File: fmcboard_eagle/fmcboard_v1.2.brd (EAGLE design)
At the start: 125 x 74 mm, 113 parts, among them IC1 OPA699ID, IC10 LTC6229IMS8E#TRPBF, IC2 LM2662M_NOPB, IC3 LTC6229IMS8E#TRPBF, IC4 LTC6229IMS8E#TRPBF, IC5 LM358, IC6 OPA699ID, IC7 OPA699ID, IC8 LTC6229IMS8E#TRPBF, IC9 LTC6229IMS8E#TRPBF, J1 8pin, J12 4p-2.54, J2 ASP-134604-01, J3 4p-2.54, J4 4p-2.54, J5 8pin, J6 4p-2.54, J7 4p-2.54, U1 TXS0108EPWR

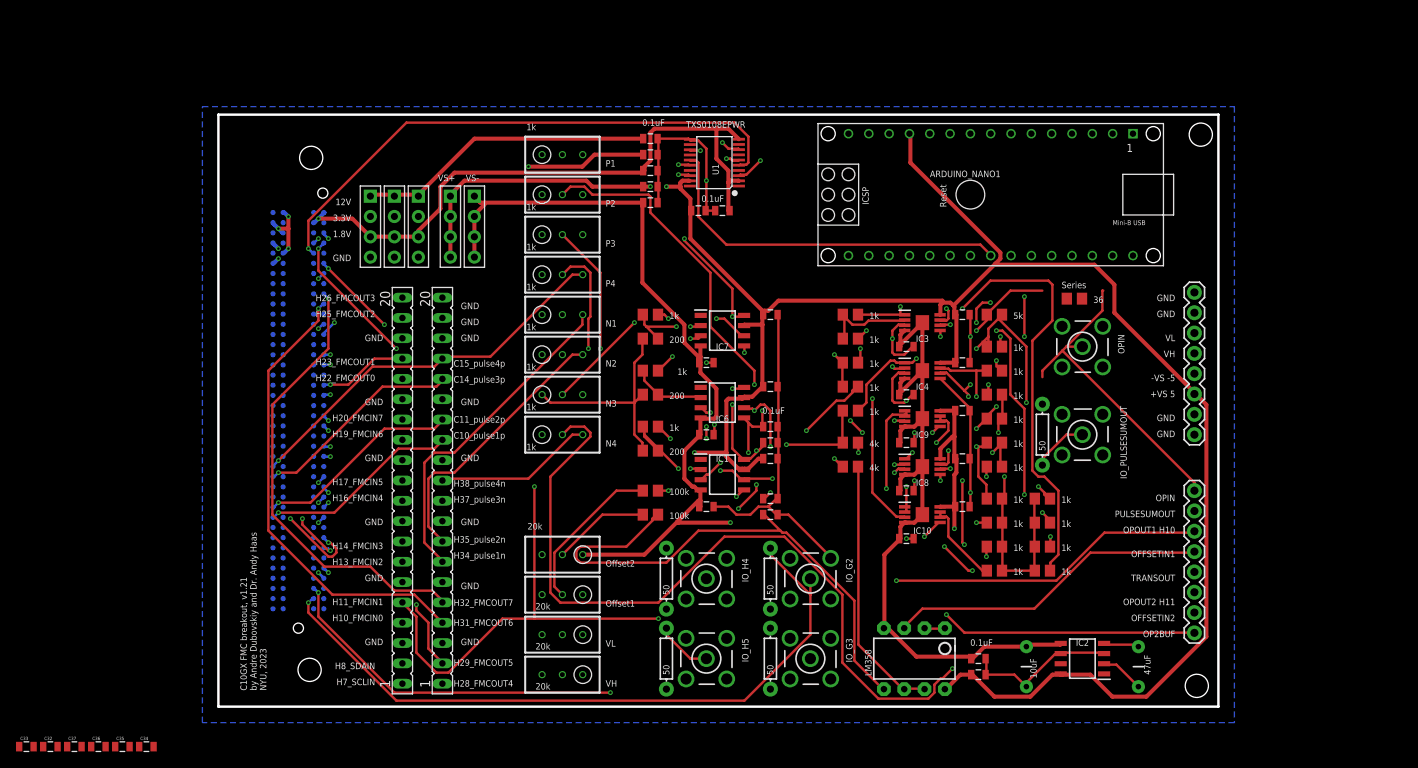
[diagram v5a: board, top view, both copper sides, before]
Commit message: cleaned up a bit, added topgnd cutouts still need to fix power, layout of amp feedback, and route
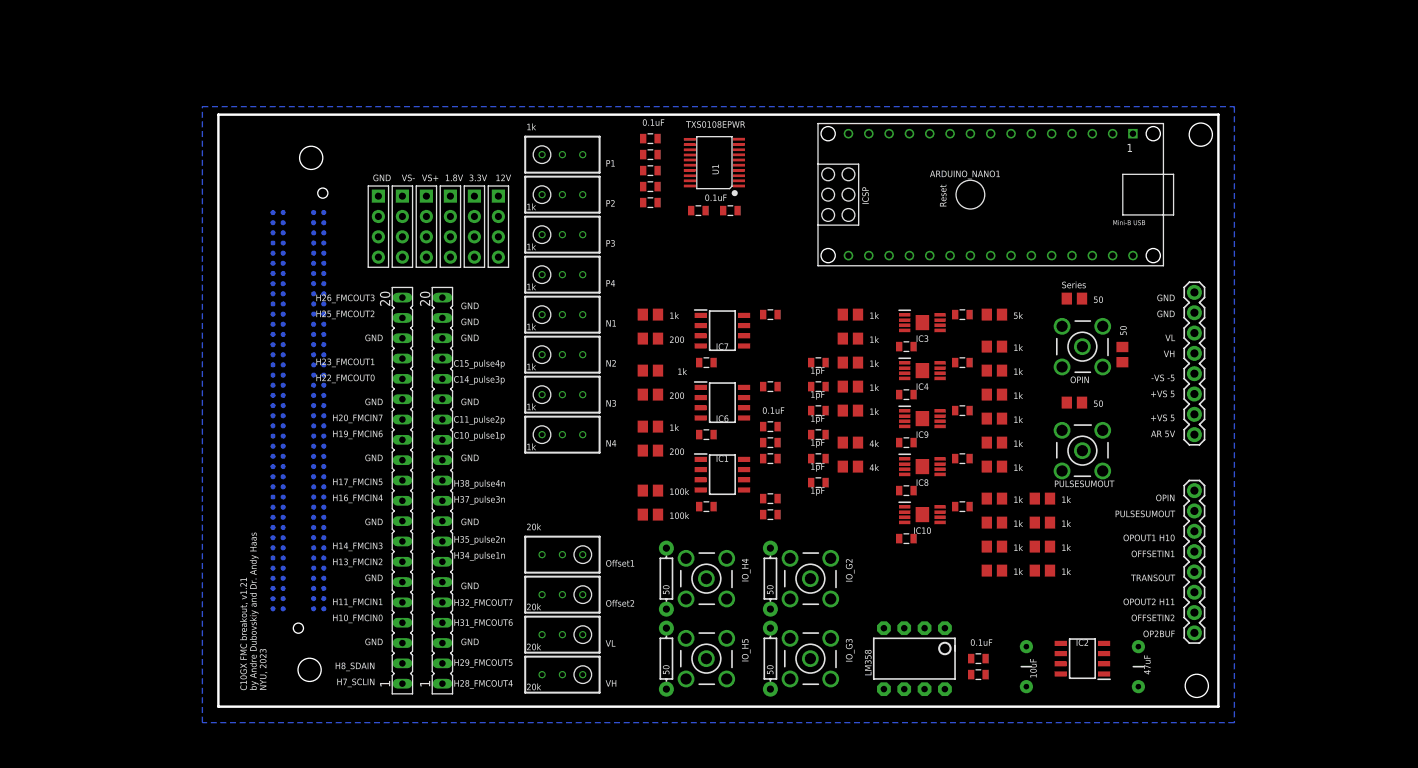
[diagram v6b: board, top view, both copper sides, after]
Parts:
- removed IO_PULSESUMOUT: BU-SMB-V, con-coax:BU-SMB-V
- added J8: 4p-2.54, Seeed-Connector:H4-2.54
- added PULSESUMOUT: BU-SMB-V, con-coax:BU-SMB-V
- added R42: 50, rcl:R0805
- C32, C34, C35, C36, C37: value 5pF -> 1pF
- R2: value 36 -> 50
- R34: device SparkFun-Resistors:AXIAL-0.3 -> rcl:R0805
- moved C33 107.5 mm to (75.0, 37.0)
- moved C32 107.3 mm to (75.0, 43.0)
- moved C37 100.8 mm to (75.0, 34.0)
- moved C36 96.9 mm to (75.0, 31.0)
- moved C34 95.3 mm to (75.0, 40.0)
- moved C35 93.0 mm to (75.0, 28.0)
- moved J12 10.0 mm to (29.0, 60.0)
- moved J7 9.00 mm to (23.0, 60.0)
- moved J3 7.00 mm to (32.0, 60.0)
- moved R34 5.66 mm to (107.0, 38.0), turned to 0 degrees
- moved R_O1 5.00 mm to (43.0, 19.0)
- moved R_O2 5.00 mm to (43.0, 14.0)
- moved J6 3.00 mm to (26.0, 60.0)
- moved J4 2.00 mm to (20.0, 60.0)
- moved C14 1.00 mm to (64.0, 62.0)
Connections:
- new net AR_5V: ARDUINO_NANO1.12, J1.1
- net 12V: now also J8.1, J8.2, J8.3, J8.4; no longer J12.1, J3.1, J4.1
- net 1V8: now also J12.1, J12.2, J12.4; no longer J3.3, J4.3
- net 3V3: now also J3.1, J3.3, J3.4; no longer J12.2, J4.2
- net GND: now also J4.1, J4.2, J4.3, PULSESUMOUT.2, PULSESUMOUT.3, PULSESUMOUT.4, PULSESUMOUT.5, R42.2; no longer IO_PULSESUMOUT.2, IO_PULSESUMOUT.3, IO_PULSESUMOUT.4, IO_PULSESUMOUT.5, J1.1, J1.2, J12.4, J3.4
- net IO1: now also R42.1
- net N$18: now also PULSESUMOUT.1, R34.2; no longer IO_PULSESUMOUT.1, R34.P$2
- net PULSESUMOUT: now also R34.1; no longer R34.P$1
- net VS+: now also J1.2; no longer ARDUINO_NANO1.12
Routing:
- net VS+: track 347.5 -> 0.00 mm, vias 4 -> 0
- net VS-: track 279.1 -> 0.00 mm, vias 1 -> 0
- net OPOUT2_H11: track 197.0 -> 0.00 mm, vias 5 -> 0
- net GND: track 165.0 -> 0.00 mm, vias 14 -> 0
- net VH: track 148.6 -> 0.00 mm, vias 7 -> 0
- net SDAIN: track 139.7 -> 0.00 mm, vias 3 -> 0
- net OPOUT1_H10: track 138.7 -> 0.00 mm, vias 5 -> 0
- net VL: track 135.6 -> 0.00 mm, vias 6 -> 0
- net SCLIN: track 128.6 -> 0.00 mm, vias 3 -> 0
- net PULSEINN4: track 124.7 -> 0.00 mm, vias 4 -> 0
- net OFFSETIN2: track 113.1 -> 0.00 mm
- net PULSEINP1: track 94.3 -> 0.00 mm, vias 3 -> 0
- net OP2BUF: track 91.3 -> 0.00 mm, vias 5 -> 0
- net H34: track 89.1 -> 0.00 mm, vias 1 -> 0
- net G2: track 87.7 -> 0.00 mm, vias 1 -> 0
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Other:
- board text added: "AR 5V"

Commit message: did power still need to fix layout of amp feedback, and route
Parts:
- removed IC2: LM2662M_NOPB, LM2662M_NOPB:SOIC127P600X175-8N
- added C38, C39, C40, C41: 10uF, SparkFun-Capacitors:CAP-PTH-5MM
- added C42, C43, C44, C45, C46, C47: 0.1uF, SparkFun-Passives:0805
- added IC11: 7805TV, linear:TO220V
- added IC12: 7905, linear:TO220H
- added L1, L2: 10uH, rcl:6000-XXXX-RC
- C1: value 47uF -> 10uF
- moved U1 74.6 mm to (105.0, 7.00), turned to 270 degrees
- moved C1 71.6 mm to (73.0, 63.0), turned to 180 degrees
- moved C9 68.3 mm to (96.0, 4.00)
- moved C14 68.0 mm to (96.0, 2.00)
- moved C2 58.7 mm to (92.0, 63.0), turned to 0 degrees
- moved ARDUINO_NANO1 57.4 mm to (137.0, 26.0), turned to 90 degrees
- moved J1 30.5 mm to (145.0, 54.0)
- moved OPIN 11.0 mm to (119.0, 46.0)
- moved PULSESUMOUT 11.0 mm to (119.0, 33.0)
- moved R2 11.0 mm to (118.0, 52.0)
- moved R34 11.0 mm to (118.0, 39.0)
- moved C15 3.16 mm to (96.0, 9.00), turned to 180 degrees
- moved C6 3.16 mm to (96.0, 7.00), turned to 180 degrees
- moved J5 2.00 mm to (122.0, 25.0)
- moved IC5 1.00 mm to (87.0, 7.00), turned to 270 degrees
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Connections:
- new net VIN+: C39.1, C42.1, J1.5, L1.1
- new net VIN-: C40.1, C44.2, J1.7, L2.1
- net GND: now also C1.2, C2.1, C38.2, C39.2, C40.2, C41.2, C42.2, C43.2, C44.1, C45.1, C46.1, C47.2, IC11.2, IC12.1, J1.6; no longer C2.2, IC2.3, IC2.6, J1.7
- net N$5: now also C38.1, C43.1, IC11.1, L1.2; no longer C1.1, IC2.2
- net N$6: now also C41.1, C45.2, IC12.2, L2.2; no longer C1.2, IC2.4
- net VH: now also J1.3; no longer J1.5
- net VL: now also J1.4; no longer J1.6
- net VS+: now also C1.1, C47.1, IC11.3; no longer IC2.8, J1.3
- net VS-: now also C2.2, C46.2, IC12.3; no longer C2.1, IC2.5, J1.4
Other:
- board size 125 x 74 mm -> 147 x 74 mm
- board text added: "VIN+"
- board text added: "VIN-"
- board text added: "Vhigh"
- board text added: "Vlow"
- board text removed: "-VS -5"

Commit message: did power still need to fix layout of amp feedback, and route
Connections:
- net N$5 renamed VIN+CLEAN
- net N$6 renamed VIN-CLEAN
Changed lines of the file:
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@@
 <wire x1="144.62" y1="33.62" x2="145" y2="54" width="0" layer="19" extent="1-1"/>
 </signal>
-<signal name="N$5">
+<signal name="VIN+CLEAN">
 <contactref element="IC11" pad="1"/>
 <contactref element="C38" pad="1"/>
@@
 <wire x1="73.46" y1="68.46" x2="124" y2="67.5" width="0" layer="19" extent="1-1"/>
 </signal>
-<signal name="N$6">
+<signal name="VIN-CLEAN">
 <contactref element="IC12" pad="2"/>
 <contactref element="C41" pad="1"/>
